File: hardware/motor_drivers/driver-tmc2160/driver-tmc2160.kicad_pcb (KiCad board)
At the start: 4 copper layers, 30 x 27.5 mm, 55 parts, among them M1 Micro-Fit 3.0, Q1 30N06, Q2 30N06, Q3 30N06, Q4 30N06, Q5 30N06, Q6 30N06, Q7 30N06, Q8 30N06, T1 GND, T10 SCK, T11 GND, T12 DIR, T13 ENCB, T14 SDI, T15 EN, T16 ENCN, T17 SDO, T18 VCC, T2 CS0, T21 Therm, T3 DIAG0, T4 CLK, T5 STEP, T6 DIAG1, T7 12V, T8 GND, T9 ENCA, U1 TMC2160

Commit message: aonteuhasntoidanouidoenuthidntoehuid
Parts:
- removed T15: EN, corevus:LGA_Land
- removed T16: ENCN, corevus:LGA_Land
- added C12: 4.7nF, AlphaLib:0402C, F.Cu at (144.6, 76.3)
- added C13: 10nF, AlphaLib:0402C, F.Cu at (141.0, 76.3)
- added D2: Y, AlphaLib:0603LED, F.Cu at (141.9, 82.1)
- added D3: R, AlphaLib:0603LED, F.Cu at (143.3, 82.1)
- added R14: DkΩ, AlphaLib:0402R, F.Cu at (144.9, 82.1)
- added R15: EkΩ, AlphaLib:0402R, F.Cu at (144.9, 81.1)
- added R16: 1kΩ, AlphaLib:0402R, F.Cu at (138.9, 84.0)
- added R17: 200Ω, AlphaLib:0402R, F.Cu at (144.9, 83.1)
- added R5: AkΩ, AlphaLib:0402R, F.Cu at (142.8, 76.3)
- added R6: BkΩ, AlphaLib:0402R, F.Cu at (143.7, 76.3)
- added R7: CkΩ, AlphaLib:0402R, F.Cu at (145.5, 76.3)
- added T19: ENCA, corevus:LGA_Land, B.Cu at (165.1, 90.3)
- added T20: ENCB, corevus:LGA_Land, B.Cu at (162.9, 90.3)
- added U2: LM393, Package_SO:MSOP-8_3x3mm_P0.65mm, F.Cu at (142.7, 79.0)
- D1: value Red -> G
- T1: moved to B.Cu
- T10: value SCK -> CS0; moved to B.Cu
- T11: value GND -> STEP; moved to B.Cu
- T12: value DIR -> GND; moved to B.Cu
- T13: value ENCB -> DIR; moved to B.Cu
- T14: value SDI -> EN; moved to B.Cu
- T17: value SDO -> DIAG0; moved to B.Cu
- T18: value VCC -> DIAG1; moved to B.Cu
- T2: value CS0 -> CLK; moved to B.Cu
- T21: value Therm -> ENCN; moved to B.Cu
- T3: value DIAG0 -> 12V; moved to B.Cu
- T4: value CLK -> SCK; moved to B.Cu
- T5: value STEP -> GND; moved to B.Cu
- T6: value DIAG1 -> SDI; moved to B.Cu
- T7: value 12V -> SDO; moved to B.Cu
- T8: value GND -> VCC; moved to B.Cu
- T9: value ENCA -> Therm; moved to B.Cu
- TH1: value 10kΩ 3380K -> 10kΩ 3950K
- moved T7 32.7 mm to (135.0, 84.2), turned to 180 degrees
- moved T2 28.4 mm to (129.0, 84.2), turned to 180 degrees
- moved T4 28.1 mm to (133.5, 84.2), turned to 180 degrees
- moved T6 27.8 mm to (138.0, 84.2), turned to 180 degrees
- moved T3 27.6 mm to (132.0, 84.2), turned to 180 degrees
- moved T5 27.3 mm to (136.5, 84.2), turned to 180 degrees
- moved T1 25.0 mm to (130.5, 84.2), turned to 180 degrees
- moved T14 22.0 mm to (144.5, 79.5), turned to 90 degrees
- moved T13 19.9 mm to (144.5, 78.0), turned to 90 degrees
- moved T12 18.0 mm to (144.5, 76.5), turned to 90 degrees
- moved T11 16.2 mm to (144.5, 75.0), turned to 90 degrees
- moved T18 16.1 mm to (146.0, 75.0), turned to -90 degrees
- moved T9 15.9 mm to (141.0, 84.2), turned to 180 degrees
- moved T8 15.3 mm to (139.5, 84.2), turned to 180 degrees
- moved T10 13.7 mm to (144.5, 81.0), turned to 90 degrees
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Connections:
- R1 pad 2: /_{M0}~{En} -> /~{En}
- R2 pad 2: /_{M0}~{En} -> /~{En}
- T10 pad 1: /SCK -> /~{CS}
- T11 pad 1: GND -> /Step
- T12 pad 1: /Dir -> GND
- T13 pad 1: /ENCB -> /Dir
- T14 pad 1: /SDI -> /~{En}
- T17 pad 1: /SDO -> /Diag0
- T18 pad 1: VCC -> /Diag1
- T2 pad 1: /~{CS} -> /Clk
- T21 pad 1: /THERM -> /ENCN
- T3 pad 1: /Diag0 -> +12V
- T4 pad 1: /Clk -> /SCK
- T5 pad 1: /Step -> GND
- T6 pad 1: /Diag1 -> /SDI
- T7 pad 1: +12V -> /SDO
- T8 pad 1: GND -> VCC
- T9 pad 1: /ENCA -> /THERM
- U1 pad 17: /_{M0}Step -> /Step
- U1 pad 18: /_{M0}Dir -> /Dir
- U1 pad 26: /_{M0}Stall -> /Diag0
- U1 pad 27: unconnected-(U1-DIAG1-Pad27) -> /Diag1
- U1 pad 28: /_{M0}~{En} -> /~{En}
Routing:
- net /SRAH: track 0.00 -> 21.2 mm, vias 0 -> 2
- net /SRAL: track 0.00 -> 20.8 mm, vias 0 -> 2
- net Net-(U1-VCC): track 1.15 -> 20.8 mm
- net VCC: track 0.00 -> 13.5 mm
- net /SRBL: track 0.00 -> 10.2 mm, vias 0 -> 2
- net Net-(U2A--): track 0.00 -> 9.59 mm
- net /SRBH: track 0.00 -> 9.47 mm, vias 0 -> 2
- net Net-(U2A-+): track 0.00 -> 6.72 mm
- net Net-(R14-Pad2): track 0.00 -> 5.70 mm
- net +48V: track 2.56 -> 7.03 mm
- net Net-(Q2-S-Pad1): track 0.00 -> 3.85 mm
- net Net-(Q6-S-Pad1): track 0.00 -> 3.72 mm, vias 8 -> 12
- net Net-(D3-K): track 0.00 -> 3.71 mm
- net /_{M0}~{En}: track 3.36 -> 0.00 mm
- net /LB1: track 6.36 -> 9.34 mm, vias 1 -> 2
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- added copper zone on In1.Cu, net GND
- added copper zone on In2.Cu, net GND
- added copper zone on B.Cu, net Net-(Q2-S-Pad1)
- added copper zone on B.Cu, net Net-(Q6-S-Pad1)
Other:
- board size 30 x 27.5 mm -> 30 x 26.5 mm
- board text added: "E"
- board text added: "S"
- board text added: "T"
- board text added: "TMC2160 5A 50V"
- board text added: "corevus"

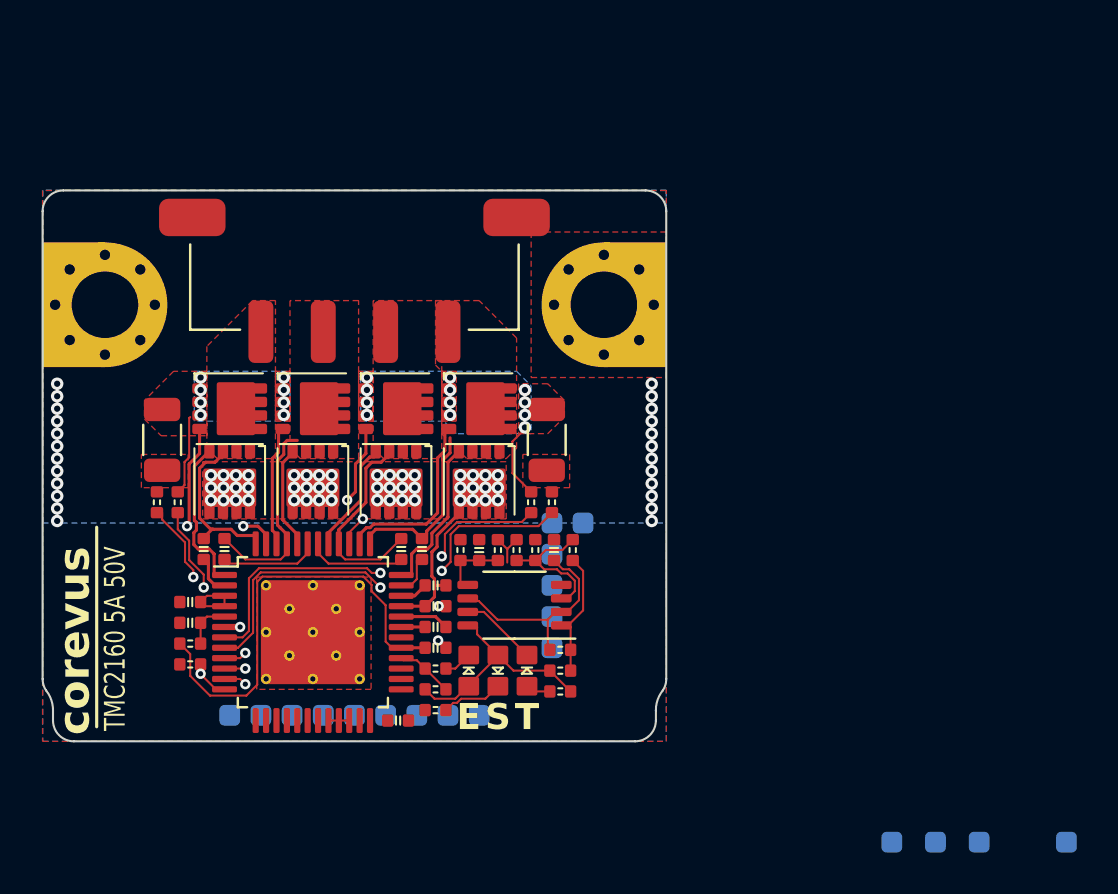
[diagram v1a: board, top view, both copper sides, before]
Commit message: v0.4 mostly complete, board needs minor revisions (e.g. pin swap)
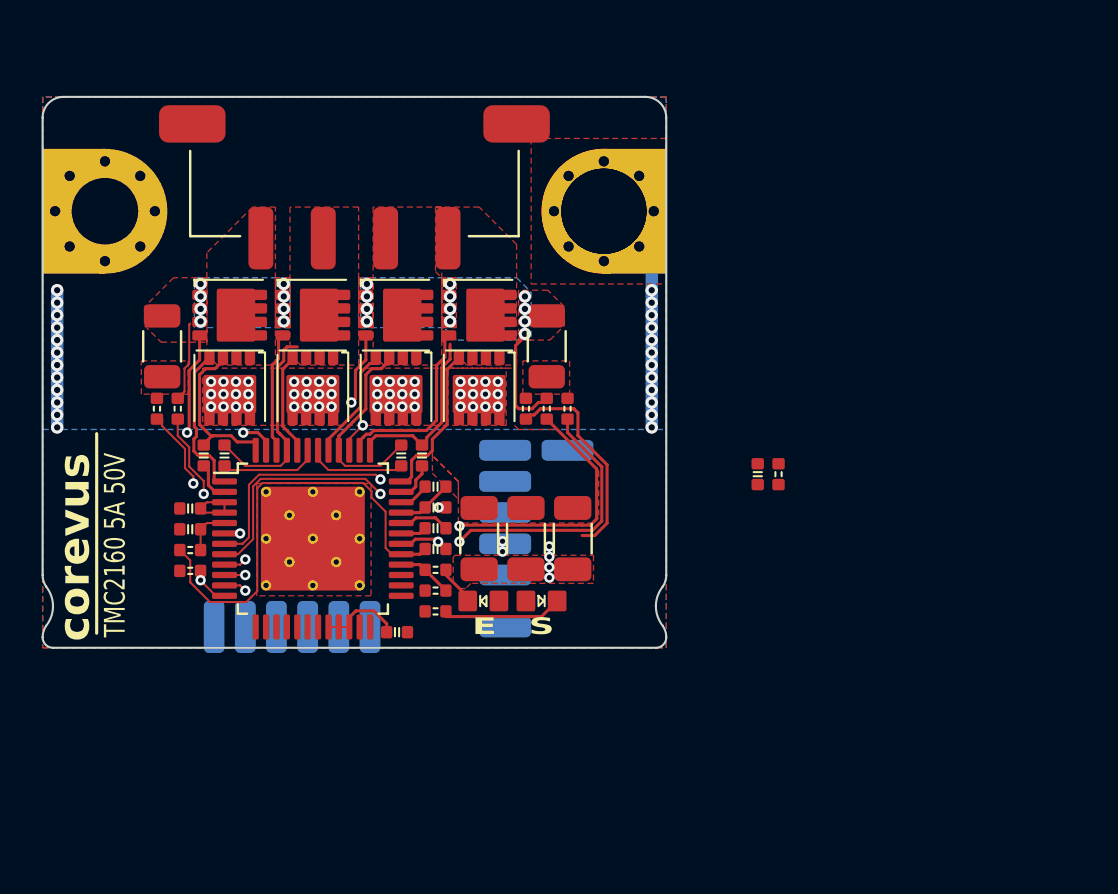
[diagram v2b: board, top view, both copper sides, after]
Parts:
- removed D3: R, AlphaLib:0603LED
- removed R14: DkΩ, AlphaLib:0402R
- removed R15: EkΩ, AlphaLib:0402R
- removed R17: 200Ω, AlphaLib:0402R
- removed R5: AkΩ, AlphaLib:0402R
- removed R6: BkΩ, AlphaLib:0402R
- removed R7: CkΩ, AlphaLib:0402R
- removed T1: GND, corevus:LGA_Land
- removed T18: DIAG1, corevus:LGA_Land
- removed T19: ENCA, corevus:LGA_Land
- removed T2: CLK, corevus:LGA_Land
- removed T20: ENCB, corevus:LGA_Land
- removed T21: ENCN, corevus:LGA_Land
- removed U2: LM393, Package_SO:MSOP-8_3x3mm_P0.65mm
- added C14: 1μF 100V, Capacitor_SMD:C_1206_3216Metric, F.Cu at (143.2, 75.8)
- added C15: 1μF 100V, Capacitor_SMD:C_1206_3216Metric, F.Cu at (145.5, 75.8)
- added H8 (x2): Gnd, corevus:M3_M2.5_PCB_Nut, F.Cu at (147.0, 60.0)
- C12: value 4.7nF -> 1μF 100V; footprint AlphaLib:0402C -> Capacitor_SMD:C_1206_3216Metric
- C13: value 10nF -> 1μF
- T10, T11, T12, T13, T14, T3, T4, T5, T6, T7, T8, T9: footprint corevus:LGA_Land -> corevus:LGA_Land_2.5mm
- T17: value DIAG0 -> DIAG; footprint corevus:LGA_Land -> corevus:LGA_Land_2.5mm
- moved T17 30.5 mm to (145.2, 71.5), turned to -90 degrees
- moved R20 14.0 mm to (155.4, 72.7)
- moved C13 13.9 mm to (154.4, 72.7)
- moved T10 9.76 mm to (142.2, 71.5)
- moved TH1 7.49 mm to (143.2, 69.5)
- moved T14 6.88 mm to (142.2, 73.0)
- moved T3 5.67 mm to (128.2, 80.0), turned to 0 degrees
- moved T4 5.67 mm to (129.8, 80.0), turned to 0 degrees
- moved T5 5.67 mm to (132.8, 80.0), turned to 0 degrees
- moved T6 5.67 mm to (134.2, 80.0), turned to 0 degrees
- moved T7 5.67 mm to (131.2, 80.0), turned to 0 degrees
- moved T8 5.67 mm to (135.8, 80.0), turned to 0 degrees
- moved C1 4.75 mm to (138.9, 73.2)
- moved C2 4.75 mm to (138.9, 75.2)
- moved C5 4.75 mm to (138.9, 76.2)
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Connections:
- C12 pad 1: Net-(U2A--) -> +48V
- T17 pad 1: /Diag0 -> /Diag
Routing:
- net GND: track 2.20 -> 20.2 mm, vias 28 -> 34
- net Net-(U2A--): track 9.59 -> 0.00 mm
- net VCC: track 13.5 -> 4.05 mm
- net /SRAL: track 20.8 -> 29.5 mm
- net /THERM: track 2.95 -> 10.1 mm
- net Net-(U2A-+): track 6.72 -> 0.00 mm
- net /SRAH: track 21.2 -> 27.8 mm
- net Net-(R14-Pad2): track 5.70 -> 0.00 mm
- net +48V: track 7.03 -> 2.67 mm
- net Net-(D3-K): track 3.71 -> 0.00 mm
- net Net-(D2-K): track 2.98 -> 5.66 mm
- net Net-(Q6-S-Pad1): track 3.72 -> 5.39 mm
- net Net-(D3-A): track 1.20 -> 0.00 mm
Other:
- outline, holes or cut-outs redrawn
- board text removed: "T"

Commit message: CvG v0.4 complete, now updating documentation
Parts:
- removed H8 (x2): Gnd, corevus:M3_M2.5_PCB_Nut
- added H3: MountingHole, corevus:ToolingHole, F.Cu at (148.0, 79.0)
- added H4: MountingHole, corevus:ToolingHole, F.Cu at (126.5, 53.5)
- added TP2: TestPoint, TestPoint:TestPoint_Pad_D1.0mm, F.Cu at (124.0, 68.0)
- added TP3: TestPoint, TestPoint:TestPoint_Pad_D1.0mm, F.Cu at (126.0, 71.8)
- added TP4: TestPoint, TestPoint:TestPoint_Pad_D1.0mm, F.Cu at (124.0, 70.0)
- M1: value Micro-Fit 3.0 -> JST XH; footprint corevus:XKB_X3025WRS-04D -> corevus:XKB_X8821WRS-04
- R1, R16: value 1kΩ -> 4.7kΩ
- moved R20 10.7 mm to (146.3, 78.2), turned to 180 degrees
- moved C13 10.4 mm to (146.3, 79.2), turned to 180 degrees
- moved T6 3.00 mm to (131.2, 80.0)
- moved T7 3.00 mm to (134.2, 80.0)
- moved M1 1.70 mm to (135.0, 57.5), turned to 180 degrees
- moved C12 0.88 mm to (141.0, 74.9)
- moved C14 0.88 mm to (143.2, 74.9)
- moved C15 0.88 mm to (145.5, 74.9)
- moved D1 0.50 mm to (141.2, 78.2)
- moved D2 0.50 mm to (144.0, 78.2)
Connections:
- M1 pad 1: /B1 -> /A2
- M1 pad 2: /B2 -> /A1
- M1 pad 3: /A1 -> /B2
- M1 pad 4: /A2 -> /B1
- T17 pad 1: /Diag -> /Diag1
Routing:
- net /~{CS}: track 0.00 -> 18.5 mm, vias 0 -> 1
- net /Diag1: track 0.00 -> 15.8 mm, vias 0 -> 1
- net VCC: track 4.05 -> 18.6 mm, vias 0 -> 2
- net /Dir: track 0.00 -> 13.1 mm, vias 0 -> 1
- net /Step: track 0.00 -> 12.1 mm, vias 0 -> 1
- net /THERM: track 10.1 -> 18.4 mm, vias 0 -> 1
- net /SDO: track 0.00 -> 7.96 mm, vias 0 -> 1
- net /~{En}: track 2.67 -> 9.95 mm, vias 0 -> 1
- net GND: track 20.2 -> 26.5 mm, vias 34 -> 39
- net +12V: track 3.01 -> 7.99 mm, vias 0 -> 1
- net /SRBH: track 9.47 -> 12.7 mm
- net /LB1: track 9.34 -> 10.8 mm, vias 2 -> 3
- net /SCK: track 0.00 -> 1.26 mm, vias 0 -> 1
- net /SRAL: track 29.5 -> 28.3 mm
- net /SRAH: track 27.8 -> 26.7 mm
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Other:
- board size 30 x 26.5 mm -> 30 x 29 mm
- board text added: "CV·24·08·19·AA"
- board text added: "JLCJLCJLCJLC"
- board text added: "NOT FOR PRODUCTION USE"
- board text added: "TMC2160 3A 48V"
- board text removed: "TMC2160 5A 50V"

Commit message: should be up to date for cvg v0.6 and latest protected drivers
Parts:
- removed H4: MountingHole, corevus:ToolingHole
- added C16: 1nF 100V, PCM_ME_passives:0402C, F.Cu at (143.0, 62.2)
- added C17: 1nF 100V, PCM_ME_passives:0402C, F.Cu at (139.0, 62.2)
- added C18: 1nF 100V, PCM_ME_passives:0402C, F.Cu at (131.0, 62.2)
- added C19: 1nF 100V, PCM_ME_passives:0402C, F.Cu at (127.0, 62.2)
- added C20: 1nF, PCM_ME_passives:0402C, F.Cu at (125.8, 70.0)
- added C21: 1nF, PCM_ME_passives:0402C, F.Cu at (144.2, 70.0)
- added D3: BAV99S, Package_TO_SOT_SMD:SOT-363_SC-70-6, F.Cu at (128.5, 60.0)
- added D4: BAV99S, Package_TO_SOT_SMD:SOT-363_SC-70-6, F.Cu at (141.5, 60.0)
- added FB1: 30Ω@100MHz, Resistor_SMD:R_0805_2012Metric, F.Cu at (141.0, 62.2)
- added FB2: 30Ω@100MHz, Resistor_SMD:R_0805_2012Metric, F.Cu at (137.0, 62.2)
- added FB3: 30Ω@100MHz, Resistor_SMD:R_0805_2012Metric, F.Cu at (133.0, 62.2)
- added FB4: 30Ω@100MHz, Resistor_SMD:R_0805_2012Metric, F.Cu at (129.0, 62.2)
- C1: value 100nF 16V -> 1μF 25V
- C10, C11, C8, C9: value 1μF -> 1μF 25V
- C2: value 22nF 100V -> 100nF 100V
- D1: value G -> Red; footprint AlphaLib:0603LED -> PCM_ME_passives:0402LED
- D2: value Y -> Green; footprint AlphaLib:0603LED -> PCM_ME_passives:0402LED
- H3: value MountingHole -> ToolingHole
- J1: renamed from M1; value JST XH -> XH; footprint corevus:XKB_X8821WRS-04 -> corevus:XH_1x04_SMD_Vertical
- R10, R13: value 30mΩ -> 50mΩ
- R16: value 4.7kΩ -> 1kΩ
- R4: value 2.2Ω -> 1Ω
- moved TH1 11.0 mm to (135.0, 62.2)
- moved R20 3.83 mm to (142.5, 78.8), turned to -90 degrees
- moved C13 2.84 mm to (143.5, 78.8), turned to -90 degrees
- moved D2 2.55 mm to (141.5, 78.8), turned to -90 degrees
- moved H3 1.80 mm to (146.5, 80.0)
- moved R11 1.12 mm to (143.8, 68.5)
- moved R12 1.12 mm to (144.8, 68.5)
- moved R8 1.03 mm to (126.2, 68.5)
- moved R9 1.03 mm to (125.2, 68.5)
- moved J1 1.00 mm to (135.0, 56.5)
- moved R10 1.00 mm to (125.8, 65.5)
- moved R13 1.00 mm to (144.2, 65.5)
- moved TP2 1.00 mm to (124.0, 67.0)
- moved TP4 1.00 mm to (124.0, 69.0)
- moved D1 0.86 mm to (140.5, 78.8), turned to -90 degrees
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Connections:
- J1 pad 1: /A2 -> /A2'
- J1 pad 2: /A1 -> /A1'
- J1 pad 3: /B2 -> /B2'
- J1 pad 4: /B1 -> /B1'
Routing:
- net /THERM: track 18.4 -> 32.5 mm, vias 1 -> 3
- net /A1': track 0.00 -> 13.1 mm
- net /B2': track 0.00 -> 11.6 mm
- net VCC: track 18.6 -> 12.7 mm, vias 2 -> 1
- net +48V: track 2.67 -> 6.47 mm, vias 48 -> 50
- net /B1': track 0.00 -> 3.66 mm
- net GND: track 26.5 -> 30.1 mm, vias 39 -> 52
- net Net-(D2-K): track 5.76 -> 2.51 mm
- net /A2': track 0.00 -> 3.16 mm
- net Net-(Q6-S-Pad1): track 5.39 -> 3.03 mm
- net /SRBH: track 12.7 -> 14.4 mm
- net /SRBL: track 9.73 -> 11.4 mm
- net /~{CS}: track 18.5 -> 19.8 mm
- net /SRAH: track 26.7 -> 27.9 mm
- net /SRAL: track 28.3 -> 29.5 mm
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- added copper zone on F.Cu, net /A1'
- added copper zone on F.Cu, net /A2'
- added copper zone on F.Cu, net /B1'
- added copper zone on F.Cu, net /B2'
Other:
- outline, holes or cut-outs redrawn
- board text added: "12V"
- board text added: "3V3"
- board text added: "A"
- board text added: "CS"
- board text added: "DIR"
- board text added: "EN"
- board text added: "GND"
- board text added: "MISO"
- board text added: "MOSI"
- board text added: "NOT FOR PRODUCTION USE MERIDI ENGINEERING MAY 2024 TMC2160 STEPPER DRIVER MODULE 3.0A 48V MAX CV·24·08·19"
- board text added: "SCLK"
- board text added: "STALL"
- board text added: "STEP"
- board text added: "THERM"
- board text added: "TMC2160 48V 3.0A"
- board text removed: "CV·24·08·19·AA"
- board text removed: "JLCJLCJLCJLC"
- board text removed: "NOT FOR PRODUCTION USE"
- board text removed: "TMC2160 3A 48V"
